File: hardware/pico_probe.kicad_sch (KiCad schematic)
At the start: 24 parts

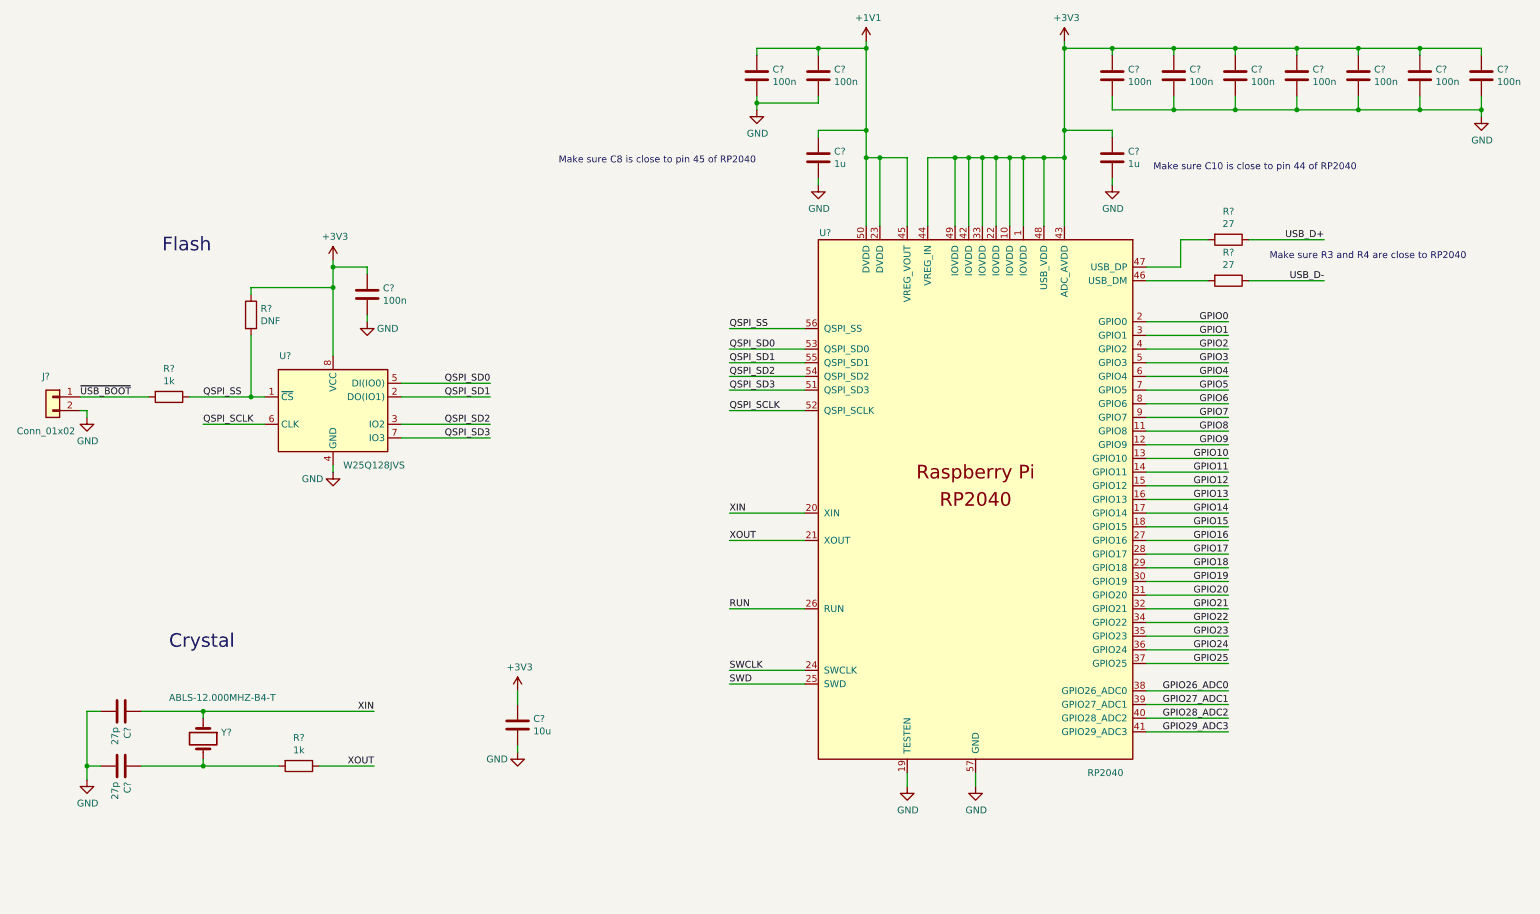
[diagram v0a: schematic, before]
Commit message: hw: Adjust minimal design schematic
- Remove GND notations
- Split power filtering capacitors to separate blocks
- Adjust desriptions in technical documentation manner
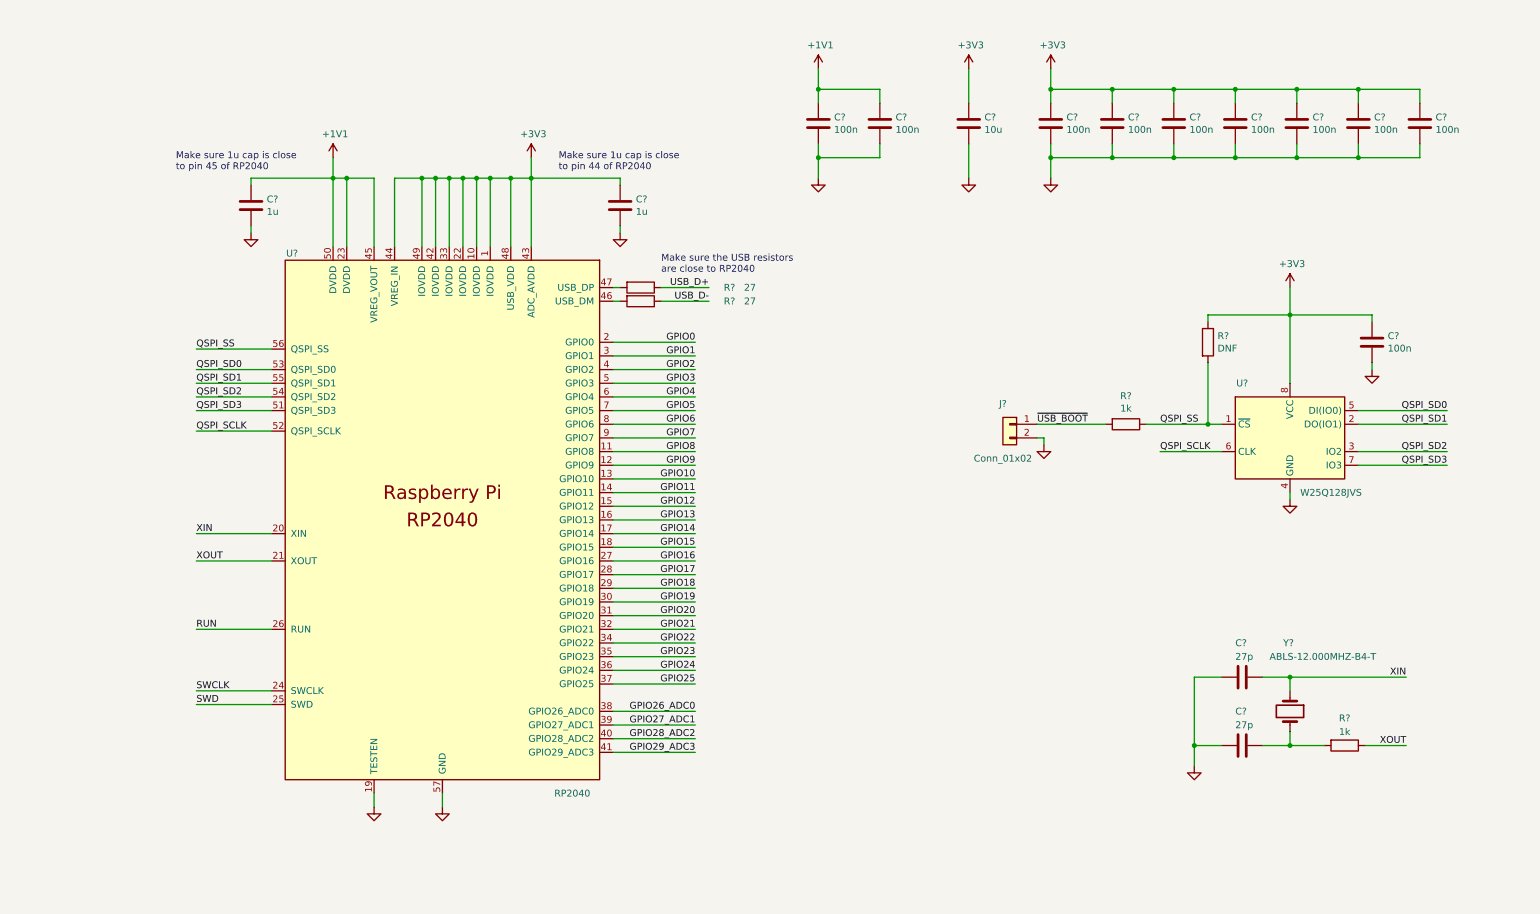
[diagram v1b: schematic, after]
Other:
- note added: "Make sure 1u cap is close to pin 44 of RP2040"
- note added: "Make sure 1u cap is close to pin 45 of RP2040"
- note added: "Make sure the USB resistors are close to RP2040"
- note removed: "Crystal"
- note removed: "Flash"
- note removed: "Make sure C10 is close to pin 44 of RP2040"
- note removed: "Make sure C8 is close to pin 45 of RP2040"
- note removed: "Make sure R3 and R4 are close to RP2040"
- moved on the sheet: C?, J?, R?, U?, Y?

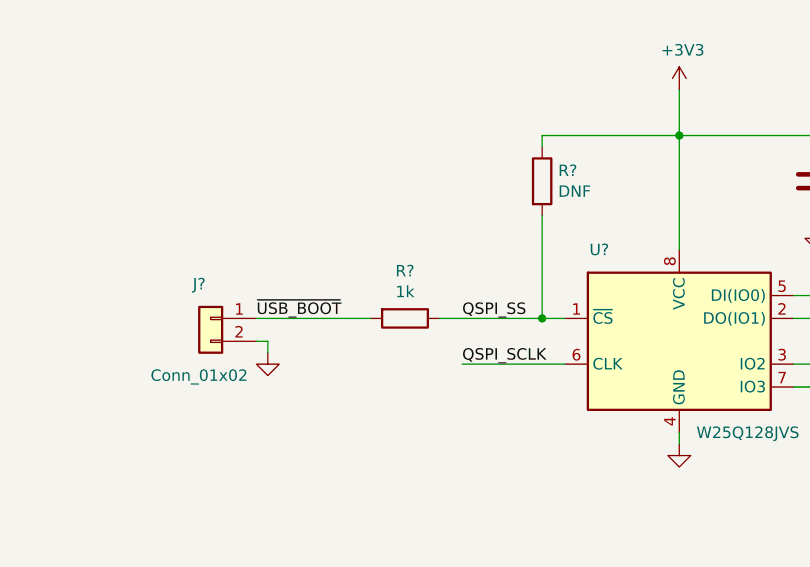
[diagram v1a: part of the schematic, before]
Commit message: hw: Add JLCPCB ordering numbers to part description
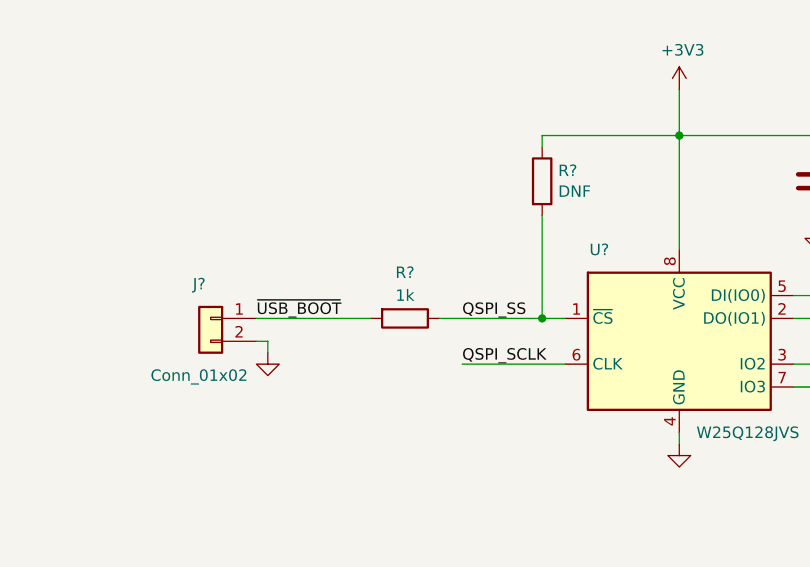
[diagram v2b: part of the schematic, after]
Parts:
- removed C? (x9): 100n, Capacitor_SMD:C_0402_1005Metric, symbol Device:C
- removed C?: 1u, Capacitor_SMD:C_0402_1005Metric, symbol Device:C
- removed C?: 27p, Capacitor_SMD:C_0402_1005Metric, symbol Device:C
- removed R?: 1k, Capacitor_SMD:C_0402_1005Metric, symbol Device:R
- removed R?: 27, Capacitor_SMD:C_0402_1005Metric, symbol Device:R
- added C? (x9): 100n, Capacitor_SMD:C_0603_1608Metric_Pad1.08x0.95mm_HandSolder, symbol Device:C
- added C?: 1u, Capacitor_SMD:C_0603_1608Metric_Pad1.08x0.95mm_HandSolder, symbol Device:C
- added C?: 27p, Capacitor_SMD:C_0603_1608Metric_Pad1.08x0.95mm_HandSolder, symbol Device:C
- added R?: 27, Capacitor_SMD:C_0603_1608Metric_Pad1.08x0.95mm_HandSolder, symbol Device:R
- added R?: 1k, Capacitor_SMD:C_0603_1608Metric_Pad1.08x0.95mm_HandSolder, symbol Device:R
- C?: footprint Capacitor_SMD:C_0402_1005Metric -> Capacitor_SMD:C_0603_1608Metric_Pad1.08x0.95mm_HandSolder; LCSC (none) -> C1656; Type (none) -> C0G; Voltage (none) -> 50 V
- C?: footprint Capacitor_SMD:C_0402_1005Metric -> Capacitor_SMD:C_0603_1608Metric_Pad1.08x0.95mm_HandSolder; LCSC (none) -> C14663; Type (none) -> X7R; Voltage (none) -> 50 V
- C?: footprint Capacitor_SMD:C_0402_1005Metric -> Capacitor_SMD:C_0603_1608Metric_Pad1.08x0.95mm_HandSolder; LCSC (none) -> C1848; Type (none) -> X7R; Voltage (none) -> 50 V
- C?: footprint Capacitor_SMD:C_0805_2012Metric -> Capacitor_SMD:C_1206_3216Metric_Pad1.33x1.80mm_HandSolder; LCSC (none) -> C13585; Type (none) -> X5R; Voltage (none) -> 50 V
- R?: footprint Capacitor_SMD:C_0402_1005Metric -> Capacitor_SMD:C_0603_1608Metric_Pad1.08x0.95mm_HandSolder; LCSC (none) -> C25190
- R?: footprint Capacitor_SMD:C_0402_1005Metric -> Capacitor_SMD:C_0603_1608Metric_Pad1.08x0.95mm_HandSolder; LCSC (none) -> C23186; Power (none) -> 0.1 W
- U?: LCSC (none) -> C97521
- U?: LCSC (none) -> C2040
- Y?: LCSC (none) -> C596818
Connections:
- net +1V1: now also C?.1, C?.1
- net +3V3: now also C?.1, C?.1, C?.1, C?.1, C?.1, C?.1, C?.1, C?.1
- net GND: now also C?.2, C?.2, C?.2, C?.2, C?.2, C?.2, C?.2, C?.2, C?.2, C?.2, C?.2
- net QSPI_SS: now also R?.1
- net USB_D-: now also R?.1
- net XIN: now also C?.1
- net ~{USB_BOOT}: now also R?.2
- net at U?.46 (USB_DM): now also R?.2

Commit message: hw: Add package library
- Add RP2040 package
- Add crystal package
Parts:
- U?: footprint RP2040_minimal:RP2040-QFN-56 -> library:RP2040-QFN-56
- Y?: footprint RP2040_minimal:Crystal_SMD_HC49-US -> library:Crystal_SMD_HC49-US
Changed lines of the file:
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@@
     (property "Reference" "U?" (id 0) (at 60.96 60.96 0))
     (property "Value" "RP2040" (id 1) (at 113.03 161.29 0))
-    (property "Footprint" "RP2040_minimal:RP2040-QFN-56" (id 2) (at 69.85 110.49 0)
+    (property "Footprint" "library:RP2040-QFN-56" (id 2) (at 69.85 110.49 0)
       (effects (font (size 1.27 1.27)) hide)
     )
@@
       (effects (font (size 1.27 1.27)) (justify left))
     )
-    (property "Footprint" "RP2040_minimal:Crystal_SMD_HC49-US" (id 2) (at 246.38 146.05 0)
+    (property "Footprint" "library:Crystal_SMD_HC49-US" (id 2) (at 246.38 146.05 0)
       (effects (font (size 1.27 1.27)) hide)
     )
@@
     )
     (path "/899a4caf-0563-4c2a-9bca-5aa28747ef75"
-      (reference "U?") (unit 1) (value "RP2040") (footprint "RP2040_minimal:RP2040-QFN-56")
+      (reference "U?") (unit 1) (value "RP2040") (footprint "library:RP2040-QFN-56")
     )
     (path "/f56e10b5-909a-4bf7-b9bb-b5663dc8fff0"
-      (reference "Y?") (unit 1) (value "ABLS-12.000MHZ-B4-T") (footprint "RP2040_minimal:Crystal_SMD_HC49-US")
-    )
-  )
+      (reference "Y?") (unit 1) (value "ABLS-12.000MHZ-B4-T") (footprint "library:Crystal_SMD_HC49-US")
+    )
+  )

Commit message: hw: Add Crystal and USB-C library
- Add USB-C library package containing HRO TYPE-C-31-M-12
- Add Crystal library for ABLS-12.000MHZ-B4-T
- Remove "minimal design" crystal library
- Reorder library folder structure, separate folder for each component
  group
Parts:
- U?: footprint library:RP2040-QFN-56 -> RP2040:RP2040-QFN-56
- Y?: footprint library:Crystal_SMD_HC49-US -> ABLS:HC_49US-_AT49__1
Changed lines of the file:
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@@
     (property "Reference" "U?" (id 0) (at 60.96 60.96 0))
     (property "Value" "RP2040" (id 1) (at 113.03 161.29 0))
-    (property "Footprint" "library:RP2040-QFN-56" (id 2) (at 69.85 110.49 0)
+    (property "Footprint" "RP2040:RP2040-QFN-56" (id 2) (at 69.85 110.49 0)
       (effects (font (size 1.27 1.27)) hide)
     )
@@
       (effects (font (size 1.27 1.27)) (justify left))
     )
-    (property "Footprint" "library:Crystal_SMD_HC49-US" (id 2) (at 246.38 146.05 0)
+    (property "Footprint" "ABLS:HC_49US-_AT49__1" (id 2) (at 246.38 146.05 0)
       (effects (font (size 1.27 1.27)) hide)
     )
@@
     )
     (path "/899a4caf-0563-4c2a-9bca-5aa28747ef75"
-      (reference "U?") (unit 1) (value "RP2040") (footprint "library:RP2040-QFN-56")
+      (reference "U?") (unit 1) (value "RP2040") (footprint "RP2040:RP2040-QFN-56")
     )
     (path "/f56e10b5-909a-4bf7-b9bb-b5663dc8fff0"
-      (reference "Y?") (unit 1) (value "ABLS-12.000MHZ-B4-T") (footprint "library:Crystal_SMD_HC49-US")
-    )
-  )
+      (reference "Y?") (unit 1) (value "ABLS-12.000MHZ-B4-T") (footprint "ABLS:HC_49US-_AT49__1")
+    )
+  )

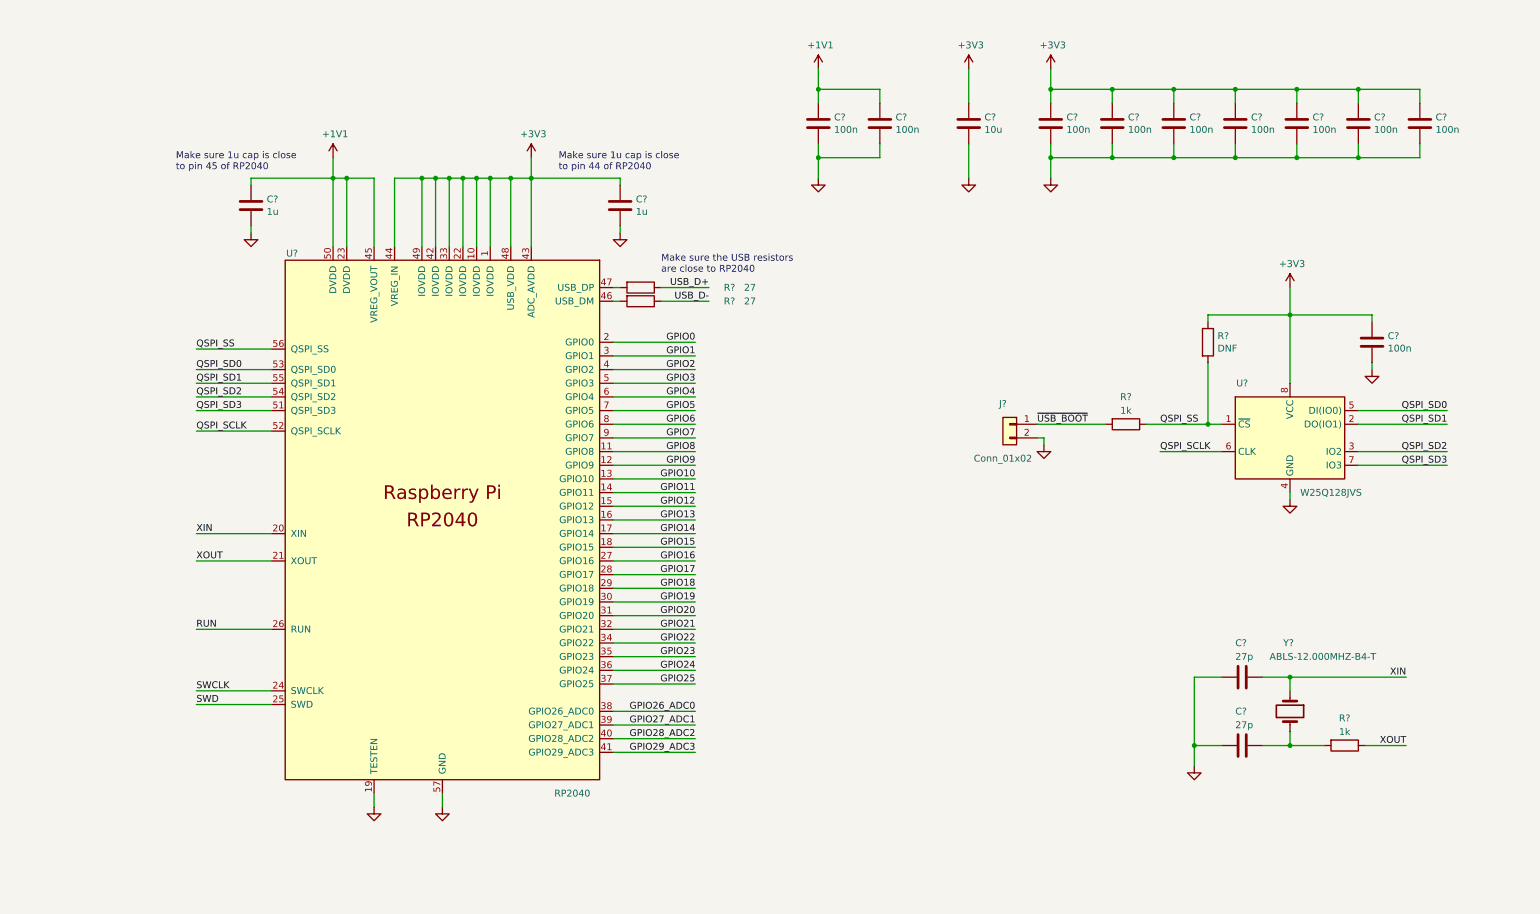
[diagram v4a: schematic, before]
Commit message: hw: Refactor schematic to hierarchical sheets
- Add sheet for procesor block
- Add sheet for power supply block
- Add sheet for interface block
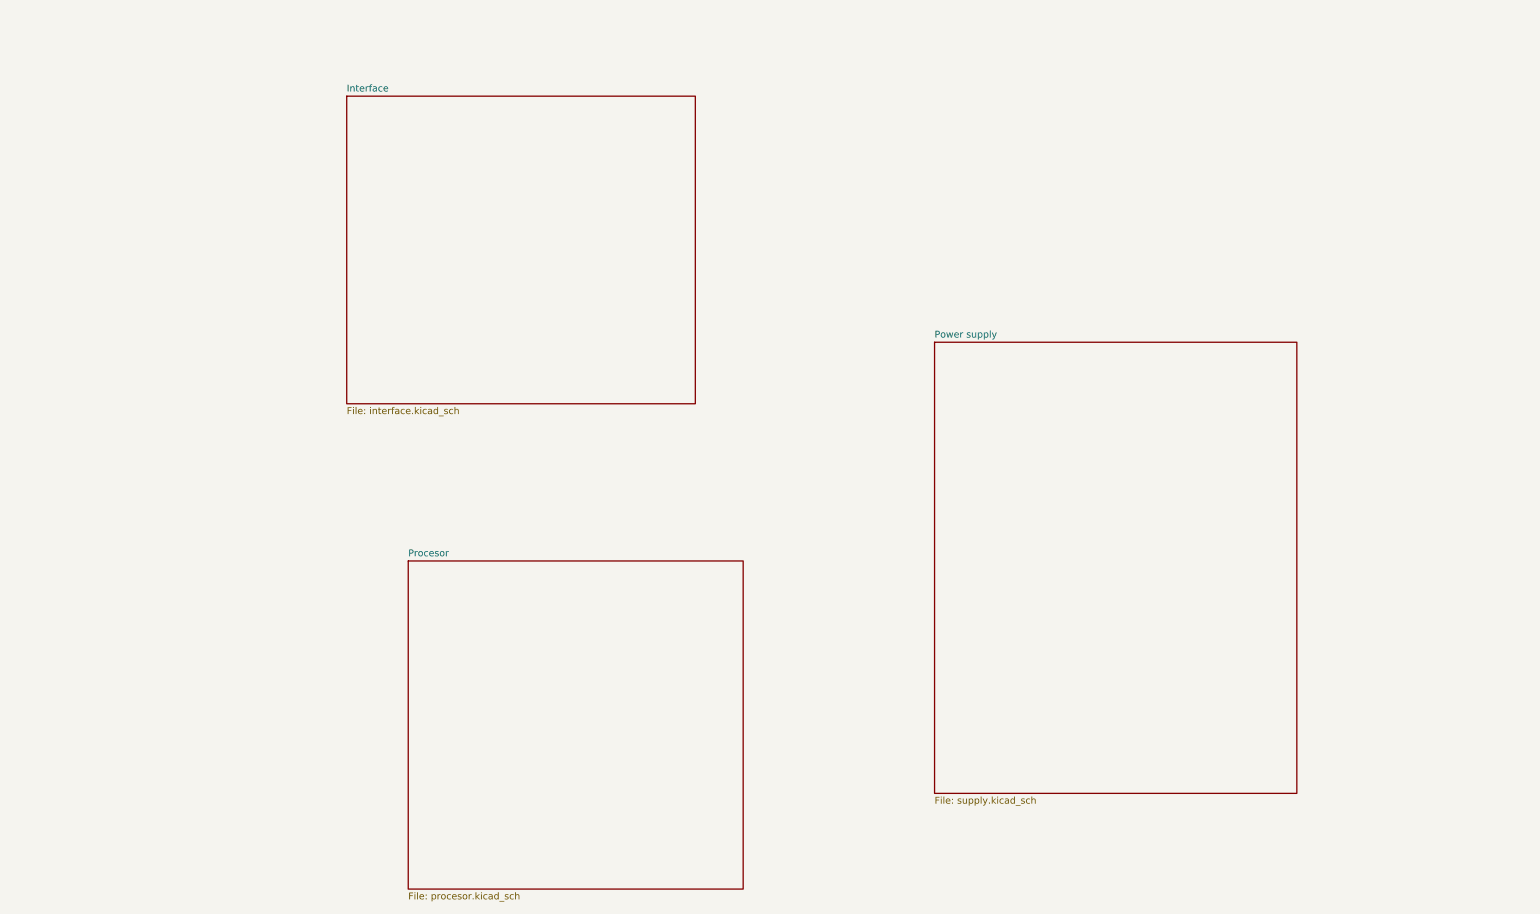
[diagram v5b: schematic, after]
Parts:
- removed C? (x2): 27p, Capacitor_SMD:C_0603_1608Metric_Pad1.08x0.95mm_HandSolder, symbol Device:C
- removed C? (x10): 100n, Capacitor_SMD:C_0603_1608Metric_Pad1.08x0.95mm_HandSolder, symbol Device:C
- removed C? (x2): 1u, Capacitor_SMD:C_0603_1608Metric_Pad1.08x0.95mm_HandSolder, symbol Device:C
- removed C?: 10u, Capacitor_SMD:C_1206_3216Metric_Pad1.33x1.80mm_HandSolder, symbol Device:C
- removed J?: Conn_01x02, Connector_PinHeader_2.54mm:PinHeader_1x02_P2.54mm_Vertical, symbol Connector_Generic:Conn_01x02
- removed R? (x2): 27, Capacitor_SMD:C_0603_1608Metric_Pad1.08x0.95mm_HandSolder, symbol Device:R
- removed R?: DNF, Capacitor_SMD:C_0402_1005Metric, symbol Device:R
- removed R? (x2): 1k, Capacitor_SMD:C_0603_1608Metric_Pad1.08x0.95mm_HandSolder, symbol Device:R
- removed U?: W25Q128JVS, Package_SO:SOIC-8_5.23x5.23mm_P1.27mm, symbol Memory_Flash:W25Q128JVS
- removed U?: RP2040, RP2040:RP2040-QFN-56, symbol MCU_RaspberryPi_RP2040:RP2040
- removed Y?: ABLS-12.000MHZ-B4-T, ABLS:HC_49US-_AT49__1, symbol Device:Crystal
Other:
- added sheet Interface (interface.kicad_sch)
- added sheet Power supply (supply.kicad_sch)
- added sheet Procesor (procesor.kicad_sch)
- note removed: "Make sure 1u cap is close to pin 44 of RP2040"
- note removed: "Make sure 1u cap is close to pin 45 of RP2040"
- note removed: "Make sure the USB resistors are close to RP2040"
